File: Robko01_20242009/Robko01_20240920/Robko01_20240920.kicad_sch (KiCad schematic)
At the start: 62 parts, among them J1 Conn_01x04_Pin, J10 Motors, J11 Motors, J12 Conn_01x04_Pin, J13 Conn_01x02_Pin, J14 Conn_01x04_Pin, J15 Conn_01x02_Pin, J16 Conn_01x04_Pin, J17 Conn_01x02_Male, J18 Conn_01x02_Male, J19 Conn_01x02_Male, J2 Conn_01x02_Pin, J21 Conn_01x19_Pin, J22 Conn_01x19_Pin, J23 Conn_01x06_Pin, J24 Conn_01x04_Pin, J25 Conn_01x04_Pin, J26 Conn_01x04_Pin, J27 Conn_01x06_Pin, J28 Conn_01x02_Male, J29 Conn_01x07_Pin, J3 Conn_01x02_Pin, J30 Conn_01x02_Male, J31 Conn_01x02_Male, J32 Conn_01x01_Pin, J34 Conn_01x01_Pin, J4 Conn_01x04_Pin, J5 Conn_01x02_Pin, J6 Conn_01x04_Pin, J7 Conn_01x02_Male, J8 Conn_01x02_Pin, J9 Motors, K1 Relay_DPDT, SW1 SW_DIP_x05, SW2 SW_DIP_x05, SW3 SW_DIP_x05, SW4 SW_DIP_x05, SW5 SW_DIP_x05, SW6 SW_DIP_x05

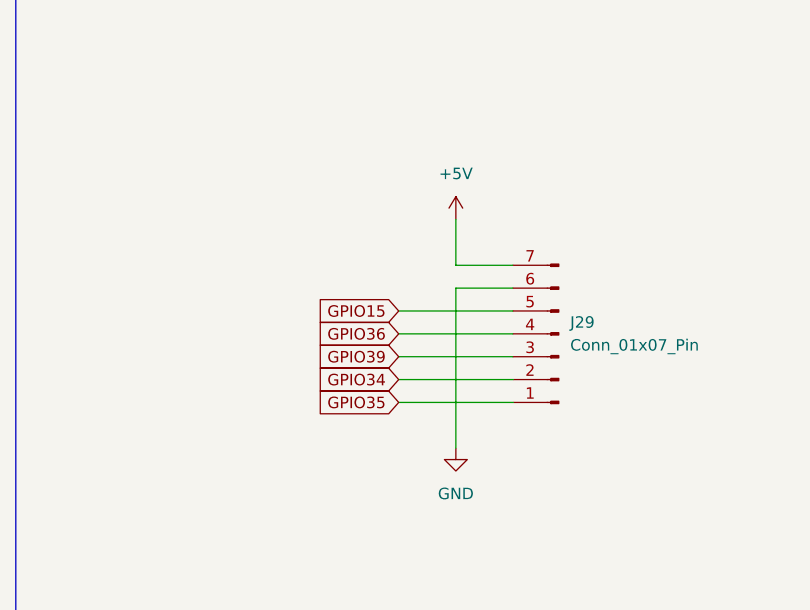
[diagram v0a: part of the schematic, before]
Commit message: Fix main MCU footprint size
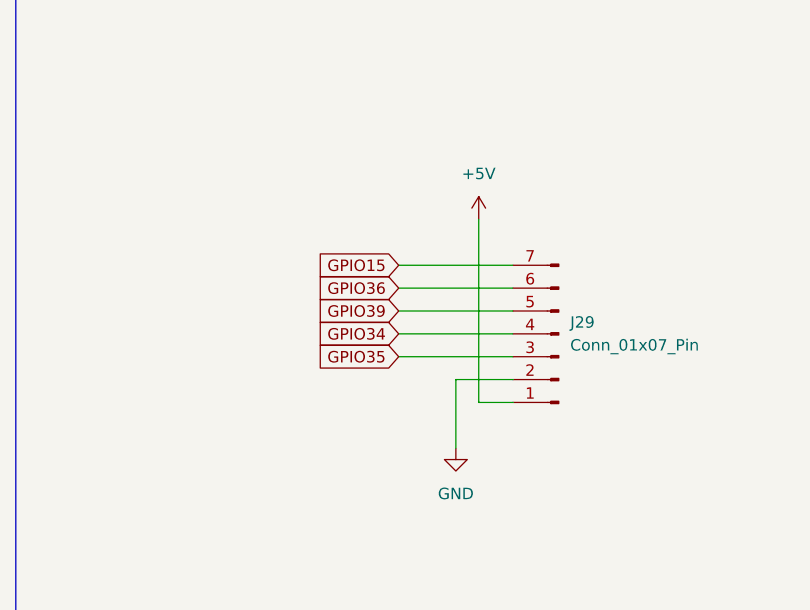
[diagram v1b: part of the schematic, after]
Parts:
- J29: footprint Connector_PinHeader_2.54mm:PinHeader_1x07_P2.54mm_Vertical -> Connector_PinHeader_2.54mm:PinHeader_1x07_P2.54mm_Horizontal
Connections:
- net +5V: now also J29.1 (Pin_1); no longer J29.7 (Pin_7)
- net GND: now also J29.2 (Pin_2); no longer J29.6 (Pin_6)
- net GPIO15: now also J29.7 (Pin_7); no longer J29.5 (Pin_5)
- net GPIO34: now also J29.4 (Pin_4); no longer J29.2 (Pin_2)
- net GPIO35: now also J29.3 (Pin_3); no longer J29.1 (Pin_1)
- net GPIO36: now also J29.6 (Pin_6); no longer J29.4 (Pin_4)
- net GPIO39: now also J29.5 (Pin_5); no longer J29.3 (Pin_3)
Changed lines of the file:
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@@
 	(wire
 		(pts
+			(xy 474.98 557.53) (xy 487.68 557.53)
+		)
+		(stroke
+			(width 0)
+			(type default)
+		)
+	)
+	(wire
+		(pts
 			(xy 629.92 487.68) (xy 633.73 487.68)
 		)
@@
 	(wire
 		(pts
+			(xy 481.33 570.23) (xy 481.33 577.85)
+		)
+		(stroke
+			(width 0)
+			(type default)
+		)
+	)
+	(wire
+		(pts
 			(xy 408.94 354.33) (xy 414.02 354.33)
 		)
@@
 	(wire
 		(pts
-			(xy 474.98 570.23) (xy 487.68 570.23)
-		)
-		(stroke
-			(width 0)
-			(type default)
-		)
-	)
-	(wire
-		(pts
 			(xy 307.34 254) (xy 311.15 254)
 		)
@@
 	(wire
 		(pts
-			(xy 474.98 572.77) (xy 487.68 572.77)
-		)
-		(stroke
-			(width 0)
-			(type default)
-		)
-	)
-	(wire
-		(pts
 			(xy 648.97 487.68) (xy 676.91 487.68)
 		)
@@
 	(wire
 		(pts
-			(xy 481.33 557.53) (xy 481.33 552.45)
-		)
-		(stroke
-			(width 0)
-			(type default)
-		)
-	)
-	(wire
-		(pts
 			(xy 718.82 372.11) (xy 718.82 368.3)
 		)
@@
 	(wire
 		(pts
-			(xy 481.33 560.07) (xy 481.33 577.85)
-		)
-		(stroke
-			(width 0)
-			(type default)
-		)
-	)
-	(wire
-		(pts
 			(xy 394.97 372.11) (xy 350.52 372.11)
 		)
@@
 	(wire
 		(pts
+			(xy 481.33 570.23) (xy 487.68 570.23)
+		)
+		(stroke
+			(width 0)
+			(type default)
+		)
+	)
+	(wire
+		(pts
 			(xy 692.15 295.91) (xy 718.82 295.91)
 		)
@@
 	(wire
 		(pts
-			(xy 487.68 560.07) (xy 481.33 560.07)
-		)
-		(stroke
-			(width 0)
-			(type default)
-		)
-	)
-	(wire
-		(pts
 			(xy 648.97 485.14) (xy 676.91 485.14)
 		)
@@
 	(wire
 		(pts
+			(xy 474.98 560.07) (xy 487.68 560.07)
+		)
+		(stroke
+			(width 0)
+			(type default)
+		)
+	)
+	(wire
+		(pts
 			(xy 472.44 344.17) (xy 485.14 344.17)
 		)
@@
 	(wire
 		(pts
+			(xy 483.87 552.45) (xy 483.87 572.77)
+		)
+		(stroke
+			(width 0)
+			(type default)
+		)
+	)
+	(wire
+		(pts
 			(xy 730.25 453.39) (xy 730.25 457.2)
 		)
@@
 	(wire
 		(pts
+			(xy 487.68 572.77) (xy 483.87 572.77)
+		)
+		(stroke
+			(width 0)
+			(type default)
+		)
+	)
+	(wire
+		(pts
 			(xy 294.64 231.14) (xy 311.15 231.14)
 		)
@@
 	(wire
 		(pts
-			(xy 487.68 557.53) (xy 481.33 557.53)
-		)
-		(stroke
-			(width 0)
-			(type default)
-		)
-	)
-	(wire
-		(pts
 			(xy 720.09 599.44) (xy 720.09 603.25)
 		)
@@
 	(global_label "GPIO39"
 		(shape input)
-		(at 474.98 567.69 180)
+		(at 474.98 562.61 180)
 		(fields_autoplaced yes)
 		(effects
@@
 		)
 		(property "Intersheetrefs" "${INTERSHEET_REFS}"
-			(at 465.1005 567.69 0)
+			(at 465.1005 562.61 0)
 			(effects
 				(font
@@
 	(global_label "GPIO36"
 		(shape input)
-		(at 474.98 565.15 180)
+		(at 474.98 560.07 180)
 		(fields_autoplaced yes)
 		(effects
@@
 		)
 		(property "Intersheetrefs" "${INTERSHEET_REFS}"
-			(at 465.1005 565.15 0)
+			(at 465.1005 560.07 0)
 			(effects
 				(font
@@
 	(global_label "GPIO35"
 		(shape input)
-		(at 474.98 572.77 180)
+		(at 474.98 567.69 180)
 		(fields_autoplaced yes)
 		(effects
@@
 		)
 		(property "Intersheetrefs" "${INTERSHEET_REFS}"
-			(at 465.1005 572.77 0)
+			(at 465.1005 567.69 0)
 			(effects
 				(font
@@
 	(global_label "GPIO15"
 		(shape input)
-		(at 474.98 562.61 180)
+		(at 474.98 557.53 180)
 		(fields_autoplaced yes)
 		(effects
@@
 		)
 		(property "Intersheetrefs" "${INTERSHEET_REFS}"
-			(at 465.1005 562.61 0)
+			(at 465.1005 557.53 0)
 			(effects
 				(font
@@
 	(global_label "GPIO34"
 		(shape input)
-		(at 474.98 570.23 180)
+		(at 474.98 565.15 180)
 		(fields_autoplaced yes)
 		(effects
@@
 		)
 		(property "Intersheetrefs" "${INTERSHEET_REFS}"
-			(at 465.1005 570.23 0)
+			(at 465.1005 565.15 0)
 			(effects
 				(font
@@
 	(symbol
 		(lib_id "power:+5V")
-		(at 481.33 552.45 0)
+		(at 483.87 552.45 0)
 		(unit 1)
 		(exclude_from_sim no)
@@
 		(fields_autoplaced yes)
 		(property "Reference" "#PWR044"
-			(at 481.33 556.26 0)
+			(at 483.87 556.26 0)
 			(effects
 				(font
@@
 		)
 		(property "Value" "+5V"
-			(at 481.33 547.37 0)
+			(at 483.87 547.37 0)
 			(effects
 				(font
@@
 		)
 		(property "Footprint" ""
-			(at 481.33 552.45 0)
+			(at 483.87 552.45 0)
 			(effects
 				(font
@@
 		)
 		(property "Datasheet" ""
-			(at 481.33 552.45 0)
+			(at 483.87 552.45 0)
 			(effects
 				(font
@@
 		)
 		(property "Description" "Power symbol creates a global label with name \"+5V\""
-			(at 481.33 552.45 0)
+			(at 483.87 552.45 0)
 			(effects
 				(font
@@
 			)
 		)
-		(property "Footprint" "Connector_PinHeader_2.54mm:PinHeader_1x07_P2.54mm_Vertical"
+		(property "Footprint" "Connector_PinHeader_2.54mm:PinHeader_1x07_P2.54mm_Horizontal"
 			(at 492.76 565.15 0)
 			(effects

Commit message: Fix geometry
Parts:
- removed D3: LED_Dual_Bidirectional, LED_THT:LED_D5.0mm_Clear, symbol Device:LED_Dual_Bidirectional
- removed K1: Relay_DPDT, Relay_THT:Relay_DPDT_Schrack-RT2-FormC_RM5mm, symbol Relay:Relay_DPDT
- removed SW1, SW2, SW3, SW4, SW5, SW6: SW_DIP_x05, Package_DIP:DIP-10_W7.62mm, symbol Switch:SW_DIP_x05
- added D3, D4: LED, LED_THT:LED_D5.0mm, symbol Device:LED
- added JP1, JP2, JP3, JP4, JP5, JP6: SolderJumper_2_Bridged, Jumper:SolderJumper-2_P1.3mm_Bridged2Bar_RoundedPad1.0x1.5mm, symbol Jumper:SolderJumper_2_Bridged
- added K2: G5V-2, Relay_THT:Relay_DPDT_Omron_G5V-2, symbol Relay:G5V-2
- added SW1, SW2, SW3, SW4, SW5, SW7: SW_DIP_x04, Package_DIP:DIP-8_W7.62mm, symbol Switch:SW_DIP_x04
- D1, D2: footprint Diode_THT:D_DO-41_SOD81_P5.08mm_Vertical_KathodeUp -> Diode_THT:D_DO-41_SOD81_P10.16mm_Horizontal
- R1: value 10k -> 2k
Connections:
- net +5V: now also SW1.1, SW1.2, SW1.3, SW1.4, SW2.1, SW2.2, SW2.3, SW2.4, SW3.1, SW3.2, SW3.3, SW3.4, SW4.1, SW4.2, SW4.3, SW4.4, SW5.1, SW5.2, SW5.3, SW5.4, SW7.1, SW7.2, SW7.3, SW7.4
- net VCC: now also K2.13
- net at A5.10 (MS1): now also SW4.8
- net at A5.11 (MS2): now also SW4.7
- net at A5.12 (MS3): now also SW4.6
- net at A5.13 (~{RESET}): now also JP5.1 (A)
- net at A5.14 (~{SLEEP}): now also JP5.2 (B)
- net at A5.2 (VDD): now also SW4.5
- net at A1.10 (MS1): now also SW7.8
- net at A1.11 (MS2): now also SW7.7
- net at A1.12 (MS3): now also SW7.6
- net at A1.13 (~{RESET}): now also JP1.1 (A)
- net at A1.14 (~{SLEEP}): now also JP1.2 (B)
- net at A1.2 (VDD): now also SW7.5
- net at A3.10 (MS1): now also SW2.8
- net at A3.13 (~{RESET}): now also JP3.1 (A)
- net at A3.14 (~{SLEEP}): now also JP3.2 (B)
- net at A3.2 (VDD): now also SW2.5
- net at A3.12 (MS3): now also SW2.6
- net at A3.11 (MS2): now also SW2.7
- net at D1.2 (A), J28.2 (Pin_2), J7.2 (Pin_2): now also D3.1 (K), D4.2 (A), K2.16, K2.8
- net at A2.10 (MS1): now also SW1.8
- net at A2.11 (MS2): now also SW1.7
- net at A2.12 (MS3): now also SW1.6
- net at A2.13 (~{RESET}): now also JP2.1 (A)
- net at A2.14 (~{SLEEP}): now also JP2.2 (B)
- net at A2.2 (VDD): now also SW1.5
- net at D1.1 (K), D2.1 (K): now also K2.1
- net at A4.10 (MS1): now also SW3.8
- net at A4.11 (MS2): now also SW3.7
- net at A4.12 (MS3): now also SW3.6
- net at A4.13 (~{RESET}): now also JP4.1 (A)
- net at A4.14 (~{SLEEP}): now also JP4.2 (B)
- net at A4.2 (VDD): now also SW3.5
- net at D2.2 (A), F1.2, R1.1: now also K2.9
- net at J17.1 (Pin_1), J17.2 (Pin_2): now also K2.4
- net at R1.2: now also D3.2 (A), D4.1 (K)
- net at A6.10 (MS1): now also SW5.8
- net at A6.11 (MS2): now also SW5.7
- net at A6.12 (MS3): now also SW5.6
- net at A6.13 (~{RESET}): now also JP6.1 (A)
- net at A6.14 (~{SLEEP}): now also JP6.2 (B)
- net at A6.2 (VDD): now also SW5.5

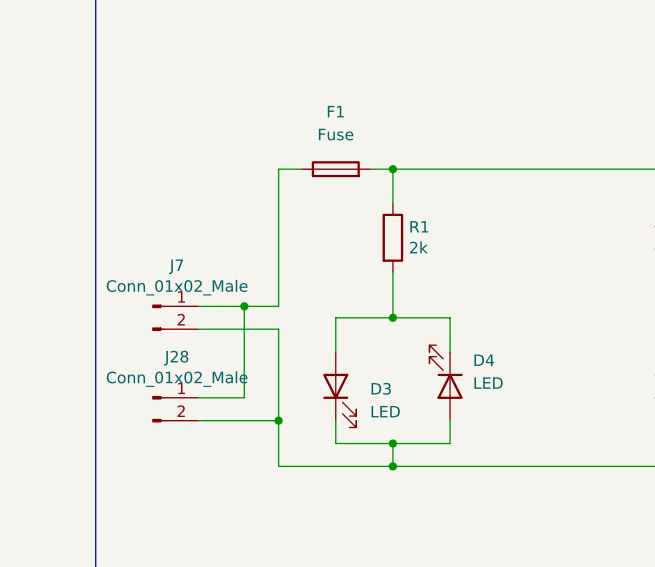
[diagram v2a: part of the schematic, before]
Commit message: Relocate elements and fix power connector positions
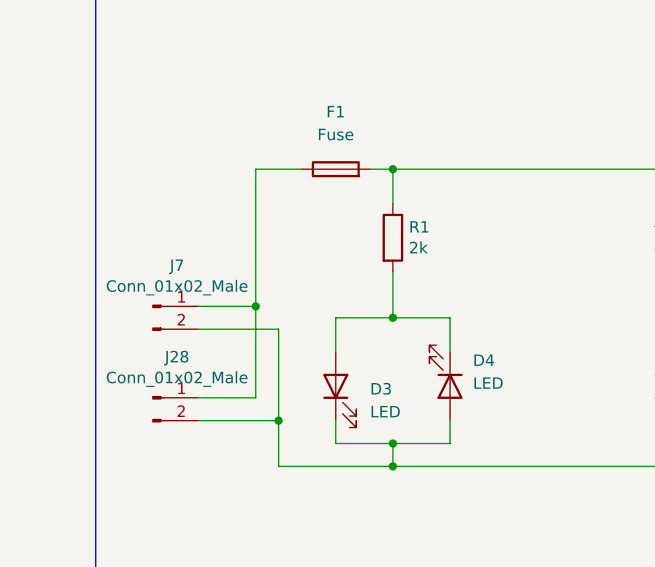
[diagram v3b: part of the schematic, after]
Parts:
- J28, J7: footprint Connector_Phoenix_MC_HighVoltage:PhoenixContact_MC_1,5_2-G-5.08_1x02_P5.08mm_Horizontal -> Connector_Phoenix_MSTB:PhoenixContact_MSTBA_2,5_2-G-5,08_1x02_P5.08mm_Horizontal
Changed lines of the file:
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@@
 	)
 	(junction
+		(at 276.86 336.55)
+		(diameter 0)
+		(color 0 0 0 0)
+	)
+	(junction
 		(at 688.34 571.5)
 		(diameter 0)
@@
 	)
 	(junction
-		(at 275.59 336.55)
-		(diameter 0)
-		(color 0 0 0 0)
-	)
-	(junction
 		(at 414.02 354.33)
 		(diameter 0)
@@
 	(wire
 		(pts
-			(xy 270.51 336.55) (xy 275.59 336.55)
+			(xy 270.51 336.55) (xy 276.86 336.55)
 		)
 		(stroke
@@
 	(wire
 		(pts
-			(xy 275.59 346.71) (xy 275.59 336.55)
+			(xy 276.86 346.71) (xy 276.86 336.55)
 		)
 		(stroke
@@
 	(wire
 		(pts
-			(xy 275.59 336.55) (xy 279.4 336.55)
-		)
-		(stroke
-			(width 0)
-			(type default)
-		)
-	)
-	(wire
-		(pts
 			(xy 629.92 482.6) (xy 633.73 482.6)
 		)
@@
 	(wire
 		(pts
-			(xy 279.4 321.31) (xy 279.4 336.55)
+			(xy 276.86 321.31) (xy 276.86 336.55)
 		)
 		(stroke
@@
 	(wire
 		(pts
-			(xy 270.51 346.71) (xy 275.59 346.71)
+			(xy 270.51 346.71) (xy 276.86 346.71)
 		)
 		(stroke
@@
 	(wire
 		(pts
-			(xy 281.94 321.31) (xy 279.4 321.31)
+			(xy 281.94 321.31) (xy 276.86 321.31)
 		)
 		(stroke
@@
 			)
 		)
-		(property "Footprint" "Connector_Phoenix_MC_HighVoltage:PhoenixContact_MC_1,5_2-G-5.08_1x02_P5.08mm_Horizontal"
+		(property "Footprint" "Connector_Phoenix_MSTB:PhoenixContact_MSTBA_2,5_2-G-5,08_1x02_P5.08mm_Horizontal"
 			(at 265.43 346.71 0)
 			(effects
@@
 			)
 		)
-		(property "Footprint" "Connector_Phoenix_MC_HighVoltage:PhoenixContact_MC_1,5_2-G-5.08_1x02_P5.08mm_Horizontal"
+		(property "Footprint" "Connector_Phoenix_MSTB:PhoenixContact_MSTBA_2,5_2-G-5,08_1x02_P5.08mm_Horizontal"
 			(at 265.43 336.55 0)
 			(effects

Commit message: Add BOM
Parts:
- added J20: Conn_01x02_Male, Connector_PinHeader_2.54mm:PinHeader_1x02_P2.54mm_Vertical, symbol Robko01-rescue:Conn_01x02_Male-Connector
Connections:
- net GND: now also J20.1 (Pin_1), J20.2 (Pin_2)
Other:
- note added: "UTILS"
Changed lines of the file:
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@@
 	)
 	(junction
+		(at 331.47 565.15)
+		(diameter 0)
+		(color 0 0 0 0)
+	)
+	(junction
 		(at 746.76 400.05)
 		(diameter 0)
@@
 	(wire
 		(pts
+			(xy 331.47 565.15) (xy 340.36 565.15)
+		)
+		(stroke
+			(width 0)
+			(type default)
+		)
+	)
+	(wire
+		(pts
 			(xy 628.65 640.08) (xy 628.65 637.54)
 		)
@@
 	(wire
 		(pts
+			(xy 331.47 562.61) (xy 331.47 565.15)
+		)
+		(stroke
+			(width 0)
+			(type default)
+		)
+	)
+	(wire
+		(pts
 			(xy 718.82 453.39) (xy 730.25 453.39)
 		)
@@
 	(wire
 		(pts
+			(xy 331.47 562.61) (xy 340.36 562.61)
+		)
+		(stroke
+			(width 0)
+			(type default)
+		)
+	)
+	(wire
+		(pts
 			(xy 749.3 392.43) (xy 749.3 397.51)
 		)
@@
 	(wire
 		(pts
+			(xy 331.47 575.31) (xy 331.47 565.15)
+		)
+		(stroke
+			(width 0)
+			(type default)
+		)
+	)
+	(wire
+		(pts
 			(xy 718.82 295.91) (xy 718.82 299.72)
 		)
@@
 	)
 	(rectangle
+		(start 259.715 520.7)
+		(end 418.465 607.695)
+		(stroke
+			(width 0)
+			(type default)
+		)
+		(fill
+			(type none)
+		)
+	)
+	(rectangle
 		(start 259.08 299.72)
 		(end 417.83 386.715)
@@
 		)
 	)
+	(text "UTILS"
+		(exclude_from_sim no)
+		(at 283.972 510.286 0)
+		(effects
+			(font
+				(size 12.7 12.7)
+			)
+		)
+	)
 	(text "Yello / Blue"
 		(exclude_from_sim no)
@@
 	)
 	(symbol
+		(lib_id "Robko01-rescue:GND-power")
+		(at 331.47 575.31 0)
+		(unit 1)
+		(exclude_from_sim no)
+		(in_bom yes)
+		(on_board yes)
+		(dnp no)
+		(property "Reference" "#PWR046"
+			(at 331.47 581.66 0)
+			(effects
+				(font
+					(size 1.27 1.27)
+				)
+				(hide yes)
+			)
+		)
+		(property "Value" "GND"
+			(at 331.597 579.7042 0)
+			(effects
+				(font
+					(size 1.27 1.27)
+				)
+			)
+		)
+		(property "Footprint" ""
+			(at 331.47 575.31 0)
+			(effects
+				(font
+					(size 1.27 1.27)
+				)
+				(hide yes)
+			)
+		)
+		(property "Datasheet" ""
+			(at 331.47 575.31 0)
+			(effects
+				(font
+					(size 1.27 1.27)
+				)
+				(hide yes)
+			)
+		)
+		(property "Description" ""
+			(at 331.47 575.31 0)
+			(effects
+				(font
+					(size 1.27 1.27)
+				)
+				(hide yes)
+			)
+		)
+		(pin "1"
+		)
+		(instances
+			(project "Robko01_20240920"
+				(path "/4cd8ddc7-060a-46ec-960d-c1cd148125cc"
+					(reference "#PWR046")
+					(unit 1)
+				)
+			)
+		)
+	)
+	(symbol
 		(lib_id "Connector:Conn_01x04_Pin")
 		(at 495.3 453.39 180)
@@
 					(unit 1)
 				)
+			)
+		)
+	)
+	(symbol
+		(lib_id "Robko01-rescue:Conn_01x02_Male-Connector")
+		(at 345.44 565.15 180)
+		(unit 1)
+		(exclude_from_sim no)
+		(in_bom yes)
+		(on_board yes)
+		(dnp no)
+		(property "Reference" "J20"
+			(at 342.7476 569.6712 0)
+			(effects
+				(font
+					(size 1.27 1.27)
+				)
+			)
+		)
+		(property "Value" "Conn_01x02_Male"
+			(at 342.7476 567.3598 0)
+			(effects
+				(font
+					(size 1.27 1.27)
+				)
+			)
+		)
+		(property "Footprint" "Connector_PinHeader_2.54mm:PinHeader_1x02_P2.54mm_Vertical"
+			(at 345.44 565.15 0)
+			(effects
+				(font
+					(size 1.27 1.27)
+				)
+				(hide yes)
+			)
+		)
+		(property "Datasheet" "~"
+			(at 345.44 565.15 0)
+			(effects
+				(font
+					(size 1.27 1.27)
+				)
+				(hide yes)
+			)
+		)
+		(property "Description" ""
+			(at 345.44 565.15 0)
+			(effects
+				(font
+					(size 1.27 1.27)
+				)
+				(hide yes)
+			)
+		)
+		(pin "1"
+		)
+		(pin "2"
+		)
+		(instances
+			(project "Robko01_20240920"
+				(path "/4cd8ddc7-060a-46ec-960d-c1cd148125cc"
+					(reference "J20")
+					(unit 1)
+				)

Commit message: Add small improvements
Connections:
- net GND: no longer J11.13 (Pin_13), J30.1 (Pin_1)
- net GRIPPER renamed GRIPPER_1
- new net GRIPPER_2: J11.13 (Pin_13), J30.1 (Pin_1)
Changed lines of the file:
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@@
 	(wire
 		(pts
-			(xy 787.4 466.09) (xy 798.83 466.09)
+			(xy 787.4 466.09) (xy 793.75 466.09)
 		)
 		(stroke
@@
 	(wire
 		(pts
-			(xy 334.01 458.47) (xy 334.01 448.31)
-		)
-		(stroke
-			(width 0)
-			(type default)
-		)
-	)
-	(wire
-		(pts
 			(xy 751.84 309.88) (xy 749.3 309.88)
 		)
@@
 	(wire
 		(pts
-			(xy 864.87 466.09) (xy 864.87 468.63)
-		)
-		(stroke
-			(width 0)
-			(type default)
-		)
-	)
-	(wire
-		(pts
 			(xy 787.4 445.77) (xy 817.88 445.77)
 		)
@@
 	(wire
 		(pts
+			(xy 862.33 466.09) (xy 867.41 466.09)
+		)
+		(stroke
+			(width 0)
+			(type default)
+		)
+	)
+	(wire
+		(pts
 			(xy 751.84 232.41) (xy 746.76 232.41)
 		)
@@
 	(wire
 		(pts
-			(xy 862.33 466.09) (xy 864.87 466.09)
-		)
-		(stroke
-			(width 0)
-			(type default)
-		)
-	)
-	(wire
-		(pts
 			(xy 657.86 467.36) (xy 657.86 500.38)
 		)
@@
 		)
 	)
-	(global_label "GRIPPER"
+	(global_label "GRIPPER_1"
 		(shape input)
-		(at 798.83 466.09 0)
+		(at 793.75 466.09 0)
 		(effects
 			(font
@@
 		)
 		(property "Intersheetrefs" "${INTERSHEET_REFS}"
-			(at 798.83 466.09 0)
+			(at 793.75 466.09 0)
 			(effects
 				(font
@@
 		)
 	)
+	(global_label "GRIPPER_2"
+		(shape input)
+		(at 334.01 448.31 180)
+		(effects
+			(font
+				(size 1.27 1.27)
+			)
+			(justify right)
+		)
+		(property "Intersheetrefs" "${INTERSHEET_REFS}"
+			(at 334.01 448.31 0)
+			(effects
+				(font
+					(size 1.27 1.27)
+				)
+				(hide yes)
+			)
+		)
+	)
 	(global_label "DIR_3"
 		(shape input)
@@
 		)
 	)
-	(global_label "GRIPPER"
+	(global_label "GRIPPER_1"
 		(shape input)
 		(at 334.01 445.77 180)
@@
 		)
 	)
+	(global_label "GRIPPER_2"
+		(shape input)
+		(at 867.41 466.09 0)
+		(effects
+			(font
+				(size 1.27 1.27)
+			)
+			(justify left)
+		)
+		(property "Intersheetrefs" "${INTERSHEET_REFS}"
+			(at 867.41 466.09 0)
+			(effects
+				(font
+					(size 1.27 1.27)
+				)
+				(hide yes)
+			)
+		)
+	)
 	(global_label "SCL"
 		(shape input)
@@
 	)
 	(symbol
-		(lib_id "Robko01-rescue:GND-power")
-		(at 864.87 468.63 0)
-		(unit 1)
-		(exclude_from_sim no)
-		(in_bom yes)
-		(on_board yes)
-		(dnp no)
-		(property "Reference" "#PWR038"
-			(at 864.87 474.98 0)
-			(effects
-				(font
-					(size 1.27 1.27)
-				)
-				(hide yes)
-			)
-		)
-		(property "Value" "GND"
-			(at 864.997 473.0242 0)
-			(effects
-				(font
-					(size 1.27 1.27)
-				)
-			)
-		)
-		(property "Footprint" ""
-			(at 864.87 468.63 0)
-			(effects
-				(font
-					(size 1.27 1.27)
-				)
-				(hide yes)
-			)
-		)
-		(property "Datasheet" ""
-			(at 864.87 468.63 0)
-			(effects
-				(font
-					(size 1.27 1.27)
-				)
-				(hide yes)
-			)
-		)
-		(property "Description" ""
-			(at 864.87 468.63 0)
-			(effects
-				(font
-					(size 1.27 1.27)
-				)
-				(hide yes)
-			)
-		)
-		(pin "1"
-		)
-		(instances
-			(project "Robko01_20240920"
-				(path "/4cd8ddc7-060a-46ec-960d-c1cd148125cc"
-					(reference "#PWR038")
-					(unit 1)
-				)
-			)
-		)
-	)
-	(symbol
 		(lib_id "Device:C_Polarized")
 		(at 731.52 610.87 0)
@@
 					(unit 1)
 				)
-			)
-		)
-	)
-	(symbol
-		(lib_id "Robko01-rescue:GND-power")
-		(at 334.01 458.47 0)
-		(unit 1)
-		(exclude_from_sim no)
-		(in_bom yes)
-		(on_board yes)
-		(dnp no)
-		(property "Reference" "#PWR045"
-			(at 334.01 464.82 0)
-			(effects
-				(font
-					(size 1.27 1.27)
-				)
-				(hide yes)
-			)
-		)
-		(property "Value" "GND"
-			(at 334.137 462.8642 0)
-			(effects
-				(font
-					(size 1.27 1.27)
-				)
-			)
-		)
-		(property "Footprint" ""
-			(at 334.01 458.47 0)
-			(effects
-				(font
-					(size 1.27 1.27)
-				)
-				(hide yes)
-			)
-		)
-		(property "Datasheet" ""
-			(at 334.01 458.47 0)
-			(effects
-				(font
-					(size 1.27 1.27)
-				)
-				(hide yes)
-			)
-		)
-		(property "Description" ""
-			(at 334.01 458.47 0)
-			(effects
-				(font
-					(size 1.27 1.27)
-				)
-				(hide yes)
-			)
-		)
-		(pin "1"
-		)
-		(instances
-			(project "Robko01_20240920"
-				(path "/4cd8ddc7-060a-46ec-960d-c1cd148125cc"
-					(reference "#PWR045")
-					(unit 1)
-				)

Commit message: Add more improvements
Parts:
- removed J17, J18, J19, J31: Conn_01x02_Male, Connector_PinHeader_2.54mm:PinHeader_1x02_P2.54mm_Vertical, symbol Robko01-rescue:Conn_01x02_Male-Connector
- removed J32, J34: Conn_01x01_Pin, symbol Connector:Conn_01x01_Pin
- added C1, C2: 100nF, Capacitor_THT:C_Disc_D7.5mm_W2.5mm_P5.00mm, symbol Device:C
- added RN1: R_Network04, Resistor_THT:R_Array_SIP5, symbol Device:R_Network04
- added U1: LM7805_TO220, Package_TO_SOT_THT:TO-220F-3_Horizontal_TabDown, symbol Regulator_Linear:LM7805_TO220
- J30: footprint Connector_PinHeader_2.54mm:PinHeader_1x02_P2.54mm_Vertical -> Connector_PinHeader_2.54mm:PinHeader_1x02_P2.54mm_Horizontal
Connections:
- net +5V: now also C2.1, U1.3 (VO)
- net GND: now also K2.4, C1.2, C2.2, U1.2 (GND)
- net GPIO34: now also RN1.4 (R3)
- net GPIO35: now also RN1.5 (R4)
- net GPIO36: now also RN1.2 (R1)
- net GPIO39: now also RN1.3 (R2)
- net GRIPPER_1: now also J30.1 (Pin_1); no longer J30.2 (Pin_2)
- net GRIPPER_2: now also J30.2 (Pin_2); no longer J30.1 (Pin_1)
- net VCC: now also C1.1, U1.1 (VI)
- net +3.3V: now reaches J21.1 (Pin_1)
- net +3.3V: now also RN1.1 (common)
- no-connect marks 21 -> 20
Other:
- moved on the sheet: J29

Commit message: Add E-Stop
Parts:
- added J17: Conn_01x02_Male, Connector_Phoenix_MSTB:PhoenixContact_MSTBA_2,5_2-G-5,08_1x02_P5.08mm_Horizontal, symbol Robko01-rescue:Conn_01x02_Male-Connector
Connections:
- net VCC: now also J17.1 (Pin_1), J17.2 (Pin_2)
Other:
- note added: "E-STOP"
